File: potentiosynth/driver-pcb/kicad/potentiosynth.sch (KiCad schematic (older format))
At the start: 13 parts, among them J1 Conn_01x40, U0 L7815

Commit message: first draft driver-pcb
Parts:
- removed R0: 10k, Resistor_SMD:R_1206_3216Metric, symbol Device:R_US
- removed R1: 47, Resistor_SMD:R_1206_3216Metric, symbol Device:R_US
- removed RV0: 1k, Potentiometer_THT:Potentiometer_Bourns_3296X_Horizontal, symbol Device:R_POT_TRIM_US
- removed TP3: TestPoint, TestPoint:TestPoint_THTPad_D3.0mm_Drill1.5mm, symbol Connector:TestPoint
- removed U0: L7815, Package_TO_SOT_THT:TO-220-3_Vertical, symbol Regulator_Linear:L7815
- added U0: R-7815-0.5, footprints:CONV_VXO7815-500-M, symbol Regulator_Switching:R-7815-0.5
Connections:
- wire segments 175 -> 155
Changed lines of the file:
@@
-	0    -1   -1   0
-$EndComp
-$Comp
-L Regulator_Linear:L7815 U0
-U 1 1 5BE47BAB
-P 1300 1650
-F 0 "U0" V 1254 1755 50  0000 L CNN
-F 1 "L7815" V 1345 1755 50  0000 L CNN
-F 2 "Package_TO_SOT_THT:TO-220-3_Vertical" H 1325 1500 50  0001 L CIN
-F 3 "" H 1300 1600 50  0001 C CNN
-	1    1300 1650
 	0    -1   -1   0
 $EndComp
@@
 Wire Wire Line
 	1300 1150 1300 1350
-Connection ~ 1300 1350
 $Comp
 L power:GND #PWR0101
@@
 	1950 1150 1750 1150
 $Comp
-L Device:R_POT_TRIM_US RV0
-U 1 1 5E22E94B
-P 3800 5350
-F 0 "RV0" H 3732 5396 50  0000 R CNN
-F 1 "1k" H 3732 5305 50  0000 R CNN
-F 2 "Potentiometer_THT:Potentiometer_Bourns_3296X_Horizontal" H 3800 5350 50  0001 C CNN
-F 3 "~" H 3800 5350 50  0001 C CNN
-	1    3800 5350
-	1    0    0    -1
-$EndComp
-$Comp
-L Device:R_US R0
-U 1 1 5E22F737
-P 3800 4850
-F 0 "R0" H 3868 4896 50  0000 L CNN
-F 1 "10k" H 3868 4805 50  0000 L CNN
-F 2 "Resistor_SMD:R_1206_3216Metric" V 3840 4840 50  0001 C CNN
-F 3 "~" H 3800 4850 50  0001 C CNN
-	1    3800 4850
-	1    0    0    -1
-$EndComp
-$Comp
-L power:+15V #PWR0106
-U 1 1 5E230106
-P 3800 4700
-F 0 "#PWR0106" H 3800 4550 50  0001 C CNN
-F 1 "+15V" H 3815 4873 50  0000 C CNN
-F 2 "" H 3800 4700 50  0001 C CNN
-F 3 "" H 3800 4700 50  0001 C CNN
-	1    3800 4700
-	1    0    0    -1
-$EndComp
-$Comp
-L power:GND #PWR0109
-U 1 1 5E230795
-P 3800 6000
-F 0 "#PWR0109" H 3800 5750 50  0001 C CNN
-F 1 "GND" H 3805 5827 50  0000 C CNN
-F 2 "" H 3800 6000 50  0001 C CNN
-F 3 "" H 3800 6000 50  0001 C CNN
-	1    3800 6000
-	1    0    0    -1
-$EndComp
-$Comp
 L power:GND #PWR0110
 U 1 1 5E30457B
@@
 $EndComp
 $Sheet
-S 4500 1750 1000 750
-U 5E3EAB60
-F0 "2" 50
-F1 "active-feedback.sch" 50
-F2 "CONTROL" I L 4500 1850 50
-F3 "ERROR" O R 5500 2050 50
-F4 "SUPPLY" O R 5500 2250 50
-F5 "RETURN" I R 5500 1850 50
-$EndSheet
-$Sheet
-S 6500 3250 1000 750
-U 5E4039E6
-F0 "6" 50
-F1 "active-feedback.sch" 50
-F2 "CONTROL" I L 6500 3350 50
-F3 "ERROR" O R 7500 3550 50
-F4 "SUPPLY" O R 7500 3750 50
-F5 "RETURN" I R 7500 3350 50
-$EndSheet
-$Sheet
 S 6500 4250 1000 750
 U 5E4039EC
 F0 "7" 50
 F1 "active-feedback.sch" 50
-F2 "CONTROL" I L 6500 4350 50
-F3 "ERROR" O R 7500 4550 50
-F4 "SUPPLY" O R 7500 4750 50
-F5 "RETURN" I R 7500 4350 50
+F2 "ERROR" O R 7500 4550 50
+F3 "COUNTER" B R 7500 4750 50
+F4 "REFERENCE" B R 7500 4350 50
 $EndSheet
 $Sheet
@@
 F0 "8" 50
 F1 "active-feedback.sch" 50
-F2 "CONTROL" I L 6500 5350 50
-F3 "ERROR" O R 7500 5550 50
-F4 "SUPPLY" O R 7500 5750 50
-F5 "RETURN" I R 7500 5350 50
+F2 "ERROR" O R 7500 5550 50
+F3 "COUNTER" B R 7500 5750 50
+F4 "REFERENCE" B R 7500 5350 50
 $EndSheet
 $Comp
@@
 	0    1    1    0
 $EndComp
-$Sheet
-S 6500 2250 1000 750
-U 5E4039E0
-F0 "5" 50
-F1 "active-feedback.sch" 50
-F2 "CONTROL" I L 6500 2350 50
-F3 "ERROR" O R 7500 2550 50
-F4 "SUPPLY" O R 7500 2750 50
-F5 "RETURN" I R 7500 2350 50
-$EndSheet
-Wire Wire Line
-	6500 2350 6400 2350
-Wire Wire Line
-	6400 5350 4400 5350
-Wire Wire Line
-	6400 5350 6500 5350
-Connection ~ 6400 5350
-Wire Wire Line
-	6500 4350 6400 4350
-Connection ~ 6400 4350
-Wire Wire Line
-	6400 4350 6400 5350
-Wire Wire Line
-	6400 2350 6400 3350
-Wire Wire Line
-	6500 3350 6400 3350
-Connection ~ 6400 3350
-Wire Wire Line
-	6400 3350 6400 4350
 $Comp
 L power:GND #PWR0104
@@
 	8250 5750 7500 5750
 Wire Wire Line
-	4400 850  4400 1850
-Connection ~ 4400 5350
-Wire Wire Line
 	7500 4350 7950 4350
 Wire Wire Line
@@
 Wire Wire Line
 	6000 1700 6000 2850
-Wire Wire Line
-	4500 3850 4400 3850
-Connection ~ 4400 3850
-Wire Wire Line
-	4400 3850 4400 5350
-Wire Wire Line
-	4500 2850 4400 2850
-Connection ~ 4400 2850
-Wire Wire Line
-	4400 2850 4400 3850
-Wire Wire Line
-	4500 1850 4400 1850
-Connection ~ 4400 1850
-Wire Wire Line
-	4400 1850 4400 2850
-$Sheet
-S 4500 2750 1000 750
-U 5E3EC44B
-F0 "3" 50
-F1 "active-feedback.sch" 50
-F2 "CONTROL" I L 4500 2850 50
-F3 "ERROR" O R 5500 3050 50
-F4 "SUPPLY" O R 5500 3250 50
-F5 "RETURN" I R 5500 2850 50
-$EndSheet
-$Sheet
-S 4500 3750 1000 750
-U 5E3ED540
-F0 "4" 50
-F1 "active-feedback.sch" 50
-F2 "CONTROL" I L 4500 3850 50
-F3 "ERROR" O R 5500 4050 50
-F4 "SUPPLY" O R 5500 4250 50
-F5 "RETURN" I R 5500 3850 50
-$EndSheet
-Wire Wire Line
-	3950 5350 4250 5350
-Wire Wire Line
-	3800 5000 3800 5200
-$Sheet
-S 4500 750  1000 750
-U 5E39B760
-F0 "1" 50
-F1 "active-feedback.sch" 50
-F2 "CONTROL" I L 4500 850 50
-F3 "ERROR" O R 5500 1050 50
-F4 "SUPPLY" O R 5500 1250 50
-F5 "RETURN" I R 5500 850 50
-$EndSheet
-Wire Wire Line
-	4400 850  4500 850
 $Comp
 L Connector:Barrel_Jack_Switch JP0
@@
 	0    -1   -1   0
 $EndComp
-$Comp
-L Connector:TestPoint TP3
-U 1 1 5DF5B544
-P 4250 5350
-F 0 "TP3" H 4250 5150 50  0000 C CNN
-F 1 "TestPoint" H 4250 5250 50  0000 C CNN
-F 2 "TestPoint:TestPoint_THTPad_D3.0mm_Drill1.5mm" H 4450 5350 50  0001 C CNN
-F 3 "~" H 4450 5350 50  0001 C CNN
-	1    4250 5350
-	1    0    0    -1
-$EndComp
-Connection ~ 4250 5350
-Wire Wire Line
-	4250 5350 4400 5350
-$Comp
-L Device:R_US R1
-U 1 1 5E2951CD
-P 3800 5850
-F 0 "R1" H 3868 5896 50  0000 L CNN
-F 1 "47" H 3868 5805 50  0000 L CNN
-F 2 "Resistor_SMD:R_1206_3216Metric" V 3840 5840 50  0001 C CNN
-F 3 "~" H 3800 5850 50  0001 C CNN
-	1    3800 5850
-	1    0    0    -1
-$EndComp
-Wire Wire Line
-	3800 5700 3800 5500
+$Sheet
+S 4500 3750 1000 750
+U 5E3ED540
+F0 "4" 50
+F1 "active-feedback.sch" 50
+F2 "ERROR" O R 5500 4050 50
+F3 "COUNTER" B R 5500 4250 50
+F4 "REFERENCE" B R 5500 3850 50
+$EndSheet
+$Sheet
+S 4500 1750 1000 750
+U 5E3EAB60
+F0 "2" 50
+F1 "active-feedback.sch" 50
+F2 "ERROR" O R 5500 2050 50
+F3 "COUNTER" B R 5500 2250 50
+F4 "REFERENCE" B R 5500 1850 50
+$EndSheet
+$Sheet
+S 4500 750  1000 750
+U 5E39B760
+F0 "1" 50
+F1 "active-feedback.sch" 50
+F2 "ERROR" O R 5500 1050 50
+F3 "COUNTER" B R 5500 1250 50
+F4 "REFERENCE" B R 5500 850 50
+$EndSheet
+$Sheet
+S 4500 2750 1000 750
+U 5E3EC44B
+F0 "3" 50
+F1 "active-feedback.sch" 50
+F2 "ERROR" O R 5500 3050 50
+F3 "COUNTER" B R 5500 3250 50
+F4 "REFERENCE" B R 5500 2850 50
+$EndSheet
+$Sheet
+S 6500 2250 1000 750
+U 5E4039E0
+F0 "5" 50
+F1 "active-feedback.sch" 50
+F2 "ERROR" O R 7500 2550 50
+F3 "COUNTER" B R 7500 2750 50
+F4 "REFERENCE" B R 7500 2350 50
+$EndSheet
+$Sheet
+S 6500 3250 1000 750
+U 5E4039E6
+F0 "6" 50
+F1 "active-feedback.sch" 50
+F2 "ERROR" O R 7500 3550 50
+F3 "COUNTER" B R 7500 3750 50
+F4 "REFERENCE" B R 7500 3350 50
+$EndSheet
+$Comp
+L Regulator_Switching:R-7815-0.5 U0
+U 1 1 60A15218
+P 1300 1650
+F 0 "U0" V 1346 1755 50  0000 L CNN
+F 1 "R-7815-0.5" V 1255 1755 50  0000 L CNN
+F 2 "footprints:CONV_VXO7815-500-M" H 1350 1400 50  0001 L CIN
+F 3 "https://www.recom-power.com/pdf/Innoline/R-78xx-0.5.pdf" H 1300 1650 50  0001 C CNN
+	1    1300 1650
+	0    -1   -1   0
+$EndComp
+Connection ~ 1300 1350
 $EndSCHEMATC

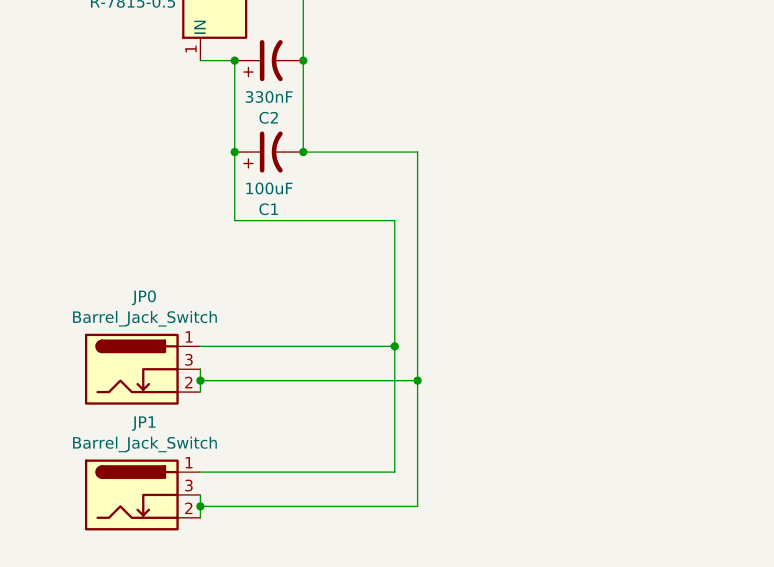
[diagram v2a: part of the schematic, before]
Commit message: add fuse
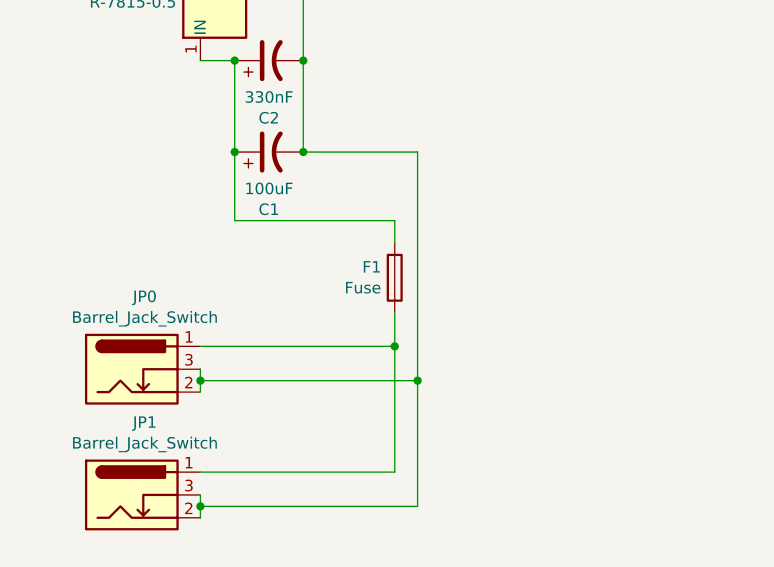
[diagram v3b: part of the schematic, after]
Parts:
- added F1: Fuse, footprints:01550900M, symbol Device:Fuse
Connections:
- net at C1.1, C2.1, U0.1 (IN): now also F1.2; no longer JP0.1, JP1.1
- new net: F1.1, JP0.1, JP1.1
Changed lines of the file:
@@
 Sheet 1 9
 Title "potentiosynth"
-Date "2021-07-07"
+Date "2021-07-09"
 Rev "B"
 Comp "University of Wisconsin-Madison"
@@
 	2150 3750 1300 3750
 Wire Wire Line
-	2150 2650 2150 3200
+	2150 2650 2150 2750
 Wire Wire Line
 	1450 2650 2150 2650
@@
 	0    -1   -1   0
 $EndComp
+$Comp
+L Device:Fuse F1
+U 1 1 60E8EB35
+P 2150 2900
+F 0 "F1" H 2091 2854 50  0000 R CNN
+F 1 "Fuse" H 2091 2945 50  0000 R CNN
+F 2 "footprints:01550900M" V 2080 2900 50  0001 C CNN
+F 3 "~" H 2150 2900 50  0001 C CNN
+	1    2150 2900
+	1    0    0    1
+$EndComp
+Wire Wire Line
+	2150 3050 2150 3200
 $EndSCHEMATC

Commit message: potentiosynth driver revC
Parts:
- C102: renamed from C2; footprint Capacitor_THT:CP_Radial_Tantal_D7.0mm_P2.50mm -> Capacitor_SMD:C_1206_3216Metric_Pad1.33x1.80mm_HandSolder; symbol Device:CP1 -> Device:C
- C103: renamed from C3; footprint Capacitor_THT:CP_Radial_Tantal_D7.0mm_P2.50mm -> Capacitor_SMD:C_1206_3216Metric_Pad1.33x1.80mm_HandSolder; symbol Device:CP1 -> Device:C
- renumbered C1 to C101
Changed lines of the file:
@@
 Sheet 1 9
 Title "potentiosynth"
-Date "2021-07-09"
+Date "2021-07-07"
 Rev "B"
 Comp "University of Wisconsin-Madison"
@@
 $EndDescr
 $Comp
-L Device:CP1 C1
+L Device:CP1 C101
 U 1 1 5BE211A8
 P 1600 2350
-F 0 "C1" V 1348 2350 50  0000 C CNN
+F 0 "C101" V 1348 2350 50  0000 C CNN
 F 1 "100uF" V 1439 2350 50  0000 C CNN
 F 2 "Capacitor_THT:CP_Radial_Tantal_D7.0mm_P2.50mm" H 1600 2350 50  0001 C CNN
@@
 	1450 2350 1450 1950
 $Comp
-L Device:CP1 C2
+L Device:C C102
 U 1 1 5BE494E1
 P 1600 1950
-F 0 "C2" V 1348 1950 50  0000 C CNN
+F 0 "C102" V 1348 1950 50  0000 C CNN
 F 1 "330nF" V 1439 1950 50  0000 C CNN
-F 2 "Capacitor_THT:CP_Radial_Tantal_D7.0mm_P2.50mm" H 1600 1950 50  0001 C CNN
+F 2 "Capacitor_SMD:C_1206_3216Metric_Pad1.33x1.80mm_HandSolder" H 1600 1950 50  0001 C CNN
 F 3 "" H 1600 1950 50  0001 C CNN
 	1    1600 1950
@@
 Wire Wire Line
 	1750 1950 1750 1650
-$Comp
-L Device:CP1 C3
-U 1 1 5BE495CB
-P 1600 1150
-F 0 "C3" V 1348 1150 50  0000 C CNN
-F 1 "100nF" V 1439 1150 50  0000 C CNN
-F 2 "Capacitor_THT:CP_Radial_Tantal_D7.0mm_P2.50mm" H 1600 1150 50  0001 C CNN
-F 3 "" H 1600 1150 50  0001 C CNN
-	1    1600 1150
-	0    -1   -1   0
-$EndComp
 Wire Wire Line
 	1750 1650 1750 1150
@@
 Wire Wire Line
 	2150 3050 2150 3200
+$Comp
+L Device:C C103
+U 1 1 5BE495CB
+P 1600 1150
+F 0 "C103" V 1348 1150 50  0000 C CNN
+F 1 "100nF" V 1439 1150 50  0000 C CNN
+F 2 "Capacitor_SMD:C_1206_3216Metric_Pad1.33x1.80mm_HandSolder" H 1600 1150 50  0001 C CNN
+F 3 "" H 1600 1150 50  0001 C CNN
+	1    1600 1150
+	0    -1   -1   0
+$EndComp
 $EndSCHEMATC
